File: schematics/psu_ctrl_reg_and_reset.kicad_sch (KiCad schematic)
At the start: 12 parts

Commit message: cleanup, fixes, started on power supplies
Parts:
- gave numbers to parts that had none: 10
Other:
- moved on the sheet: C72, C73, C78

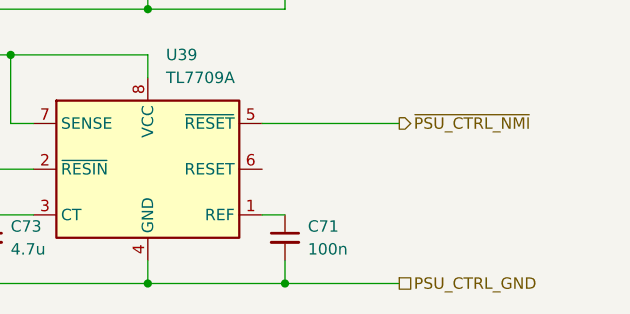
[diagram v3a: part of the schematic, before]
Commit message: Updated to KiCad v10.0. Minor improvements.
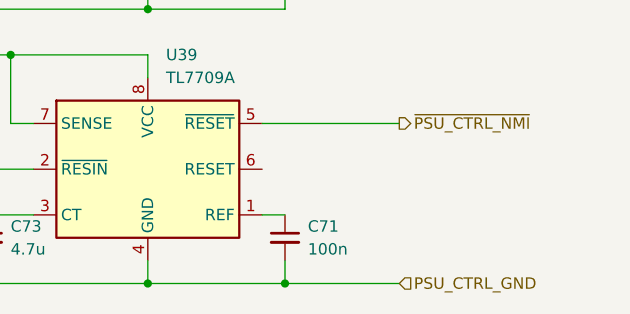
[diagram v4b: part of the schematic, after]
